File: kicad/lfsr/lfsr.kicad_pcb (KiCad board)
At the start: 2 copper layers, 25 parts, among them SW1 SW_Push, SW2 SW_Push, U1 74HC164, U2 74HC86, U3 LM7805_TO220, U4 LM555xN

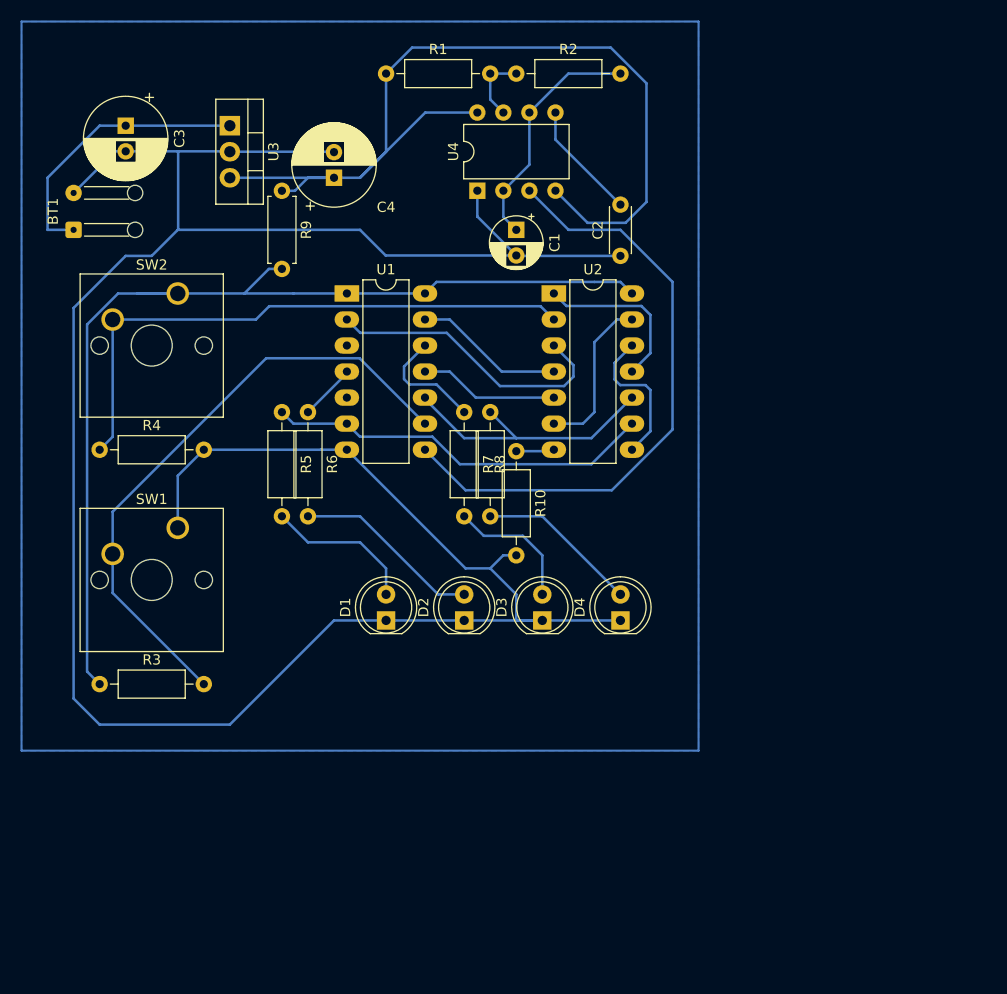
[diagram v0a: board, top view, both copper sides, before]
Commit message: Modify PCB design
Swap things around so that traces are a minimum of 1mm wide instead of 0.1mm wide. 0.1mm traces didn't perform well on the router
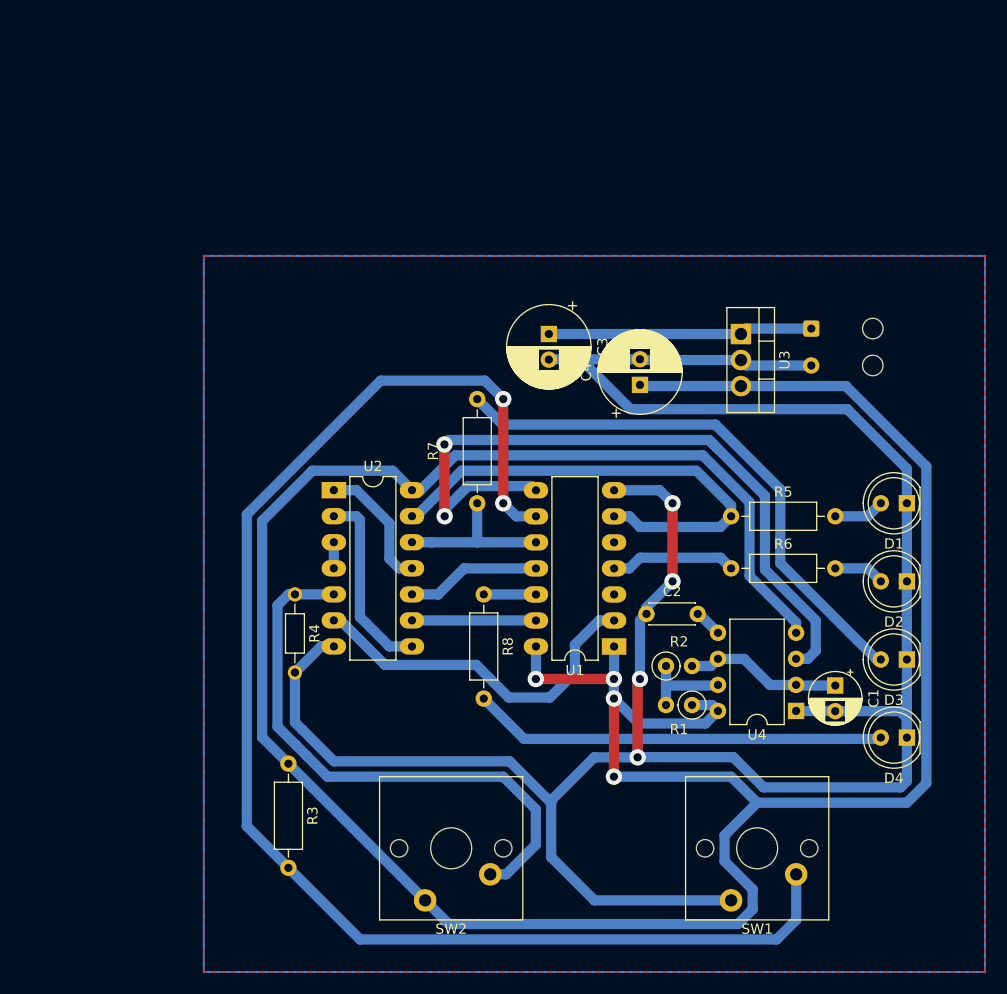
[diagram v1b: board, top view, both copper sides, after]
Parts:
- removed R10: 0Ω, Resistor_THT:R_Axial_DIN0207_L6.3mm_D2.5mm_P10.16mm_Horizontal
- removed R9: 0Ω, Resistor_THT:R_Axial_DIN0207_L6.3mm_D2.5mm_P7.62mm_Horizontal
- BT1: moved to B.Cu
- R1, R2: footprint Resistor_THT:R_Axial_DIN0207_L6.3mm_D2.5mm_P10.16mm_Horizontal -> Resistor_THT:R_Axial_DIN0207_L6.3mm_D2.5mm_P2.54mm_Vertical
- R4: footprint Resistor_THT:R_Axial_DIN0207_L6.3mm_D2.5mm_P10.16mm_Horizontal -> Resistor_THT:R_Axial_DIN0204_L3.6mm_D1.6mm_P7.62mm_Horizontal
- moved BT1 72.6 mm to (110.1, 45.2), turned to -90 degrees
- moved R1 68.4 mm to (98.4, 81.9), turned to 180 degrees
- moved SW1 65.1 mm to (102.2, 101.0), turned to 180 degrees
- moved SW2 63.9 mm to (72.4, 101.0), turned to 180 degrees
- moved R2 59.6 mm to (95.9, 78.1)
- moved U4 59.5 mm to (108.6, 82.5), turned to 180 degrees
- moved C1 54.3 mm to (112.4, 80.0)
- moved U3 53.8 mm to (103.2, 45.7)
- moved D1 52.1 mm to (119.4, 62.2), turned to 180 degrees
- moved C3 46.0 mm to (84.5, 45.7)
- moved R5 45.0 mm to (102.2, 63.5), turned to 0 degrees
- moved R6 44.0 mm to (102.2, 68.6), turned to 0 degrees
- moved D2 43.3 mm to (119.4, 69.8), turned to 180 degrees
- moved U1 43.2 mm to (90.8, 76.2), turned to 180 degrees
- moved C4 36.0 mm to (93.3, 50.7)
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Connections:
- C4 pad 1: Net-(R1-Pad1) -> Net-(R3-Pad1)
- R1 pad 1: Net-(R1-Pad1) -> Net-(R3-Pad1)
- R4 pad 1: Net-(SW2-Pad2) -> Net-(R4-Pad1)
- R5 pad 1: Net-(U1-Pad6) -> Net-(R5-Pad1)
- R7 pad 1: Net-(U1-Pad12) -> Net-(R7-Pad1)
- R8 pad 1: Net-(U1-Pad10) -> Net-(R8-Pad1)
- SW2 pad 2: Net-(SW2-Pad2) -> Net-(R4-Pad1)
- U1 pad 10: Net-(U1-Pad10) -> Net-(R7-Pad1)
- U1 pad 12: Net-(U1-Pad12) -> Net-(R8-Pad1)
- U1 pad 6: Net-(U1-Pad6) -> Net-(R5-Pad1)
- U2 pad 10: Net-(U1-Pad10) -> Net-(U1-Pad11)
- U2 pad 12: Net-(U2-Pad8) -> Net-(R7-Pad1)
- U2 pad 13: Net-(U2-Pad13) -> Net-(R5-Pad1)
- U2 pad 2: Net-(SW2-Pad2) -> Net-(U2-Pad8)
- U2 pad 3: Net-(U1-Pad2) -> Net-(U2-Pad4)
- U2 pad 4: Net-(U1-Pad13) -> Net-(U2-Pad4)
- U2 pad 5: Net-(U1-Pad11) -> Net-(R4-Pad1)
- U2 pad 6: Net-(U2-Pad13) -> Net-(U1-Pad2)
- U2 pad 9: Net-(U1-Pad6) -> Net-(U1-Pad13)
- U3 pad 3: Net-(R1-Pad1) -> Net-(R3-Pad1)
- U4 pad 4: Net-(R1-Pad1) -> Net-(R3-Pad1)
- U4 pad 8: Net-(R1-Pad1) -> Net-(R3-Pad1)
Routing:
- net Net-(R3-Pad1): track 99.5 -> 290.6 mm, vias 0 -> 4
- net Net-(R1-Pad1): track 94.1 -> 0.00 mm
- net Net-(R3-Pad2): track 59.8 -> 138.9 mm, vias 0 -> 2
- net Net-(SW2-Pad2): track 57.3 -> 0.00 mm
- net Net-(R4-Pad1): track 0.00 -> 55.4 mm
- net Net-(R5-Pad1): track 0.00 -> 47.7 mm
- net Net-(D3-Pad2): track 13.0 -> 54.1 mm
- net Net-(U1-Pad6): track 39.0 -> 0.00 mm
- net Net-(U1-Pad10): track 27.1 -> 0.00 mm
- net Net-(D4-Pad2): track 15.9 -> 40.4 mm
- net Net-(R7-Pad1): track 0.00 -> 15.9 mm
- net Net-(U2-Pad13): track 15.8 -> 0.00 mm
- net Net-(D2-Pad2): track 18.4 -> 4.97 mm
- net Net-(U1-Pad8): track 60.3 -> 72.1 mm, vias 0 -> 2
- net Net-(BT1-Pad2): track 253.9 -> 242.4 mm, vias 0 -> 4
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- added copper zone on F.Cu, net Net-(BT1-Pad2)
- added copper zone on B.Cu, net Net-(R3-Pad1)
- removed copper zone on B.Cu, net Net-(BT1-Pad2)
